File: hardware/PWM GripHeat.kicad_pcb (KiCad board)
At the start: 2 copper layers, 65 parts, among them J1 1770885, J2 1770898, J4 1770924, J5 0878340619, Q1 SiS415DNT, U1 ATtiny85-20P, U2 SiA462DJ, U3 LM324, U4 SiA462DJ

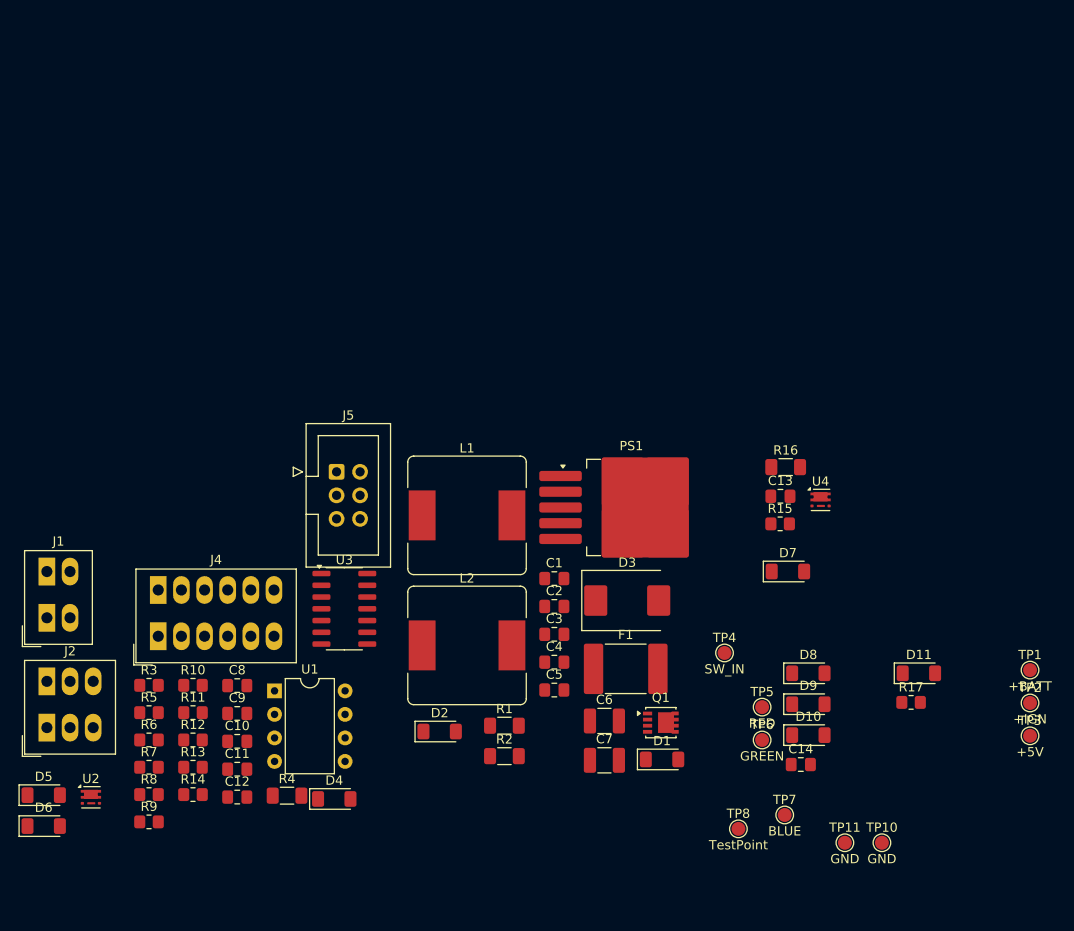
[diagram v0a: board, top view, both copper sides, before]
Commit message: PCB Basic outline
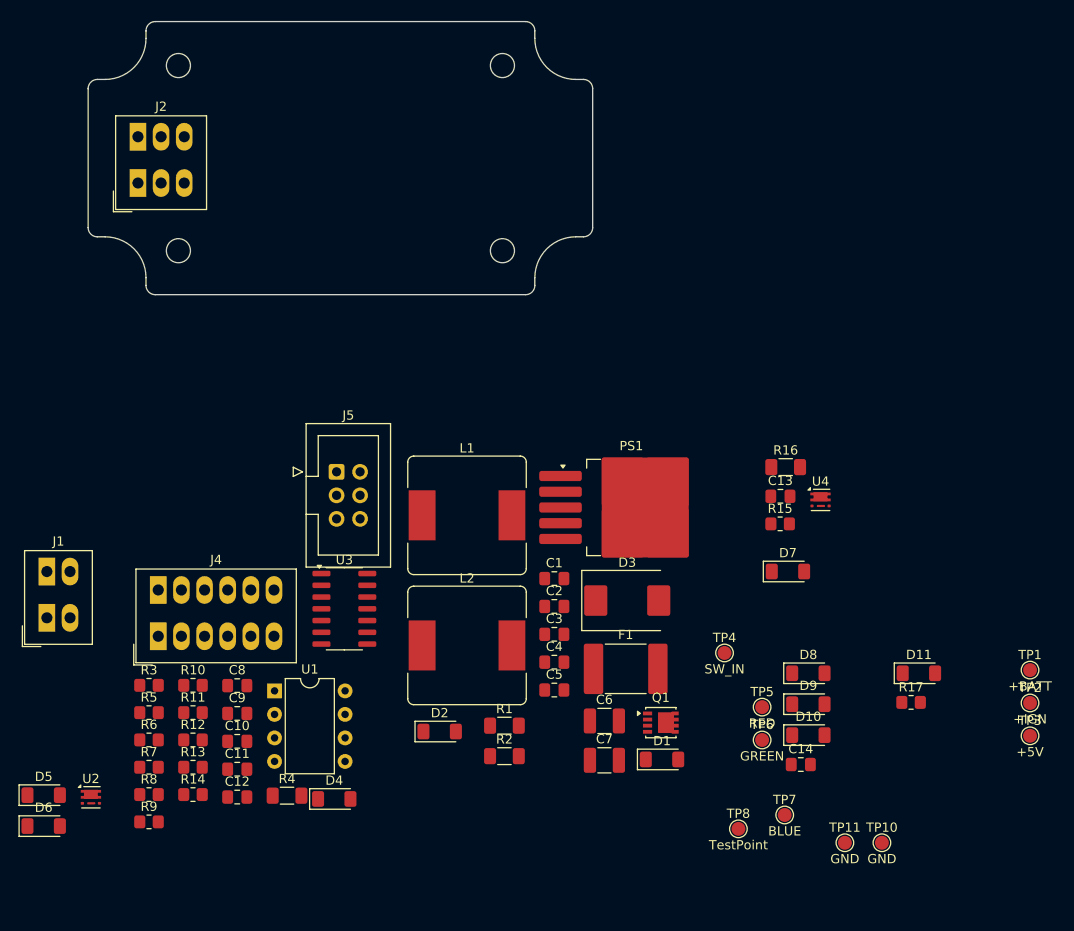
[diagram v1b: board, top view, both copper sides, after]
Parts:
- moved J2 59.6 mm to (142.1, 48.2)
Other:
- board outline added: 54.5 x 29.5 mm

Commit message: Pre DRC, almost done!
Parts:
- removed C6: EMK325ABJ107MM-T, Capacitor_SMD:C_1210_3225Metric_Pad1.33x2.70mm_HandSolder
- removed D3: B360, Diode_SMD:D_SMC
- removed D5: BZV55B18, Diode_SMD:D_MiniMELF
- removed J4: 1770924, TerminalBlock_Phoenix:TerminalBlock_Phoenix_PTSM-0,5-6-2.5-H-THR_1x06_P2.50mm_Horizontal
- removed J5: 0878340619, Connector_IDC:IDC-Header_2x03_P2.54mm_Vertical
- removed L2: 100uH, Inductor_SMD:L_Bourns_SRR1260
- removed Q1: SiS415DNT, Package_SO:Vishay_PowerPAK_1212-8_Single
- removed R1: 2.2k, Resistor_SMD:R_1206_3216Metric_Pad1.30x1.75mm_HandSolder
- removed R16: 100k, Resistor_SMD:R_1206_3216Metric_Pad1.30x1.75mm_HandSolder
- removed TP11: GND, TestPoint:TestPoint_Pad_D1.5mm
- removed U4: SiA462DJ, Package_TO_SOT_SMD:Vishay_PowerPAK_SC70-6L_Single
- added TP9: GND, TestPoint:TestPoint_THTPad_D2.0mm_Drill1.0mm, F.Cu at (138.6, 39.0)
- J1: footprint TerminalBlock_Phoenix:TerminalBlock_Phoenix_PTSM-0,5-2-2.5-H-THR_1x02_P2.50mm_Horizontal -> TerminalBlock:TerminalBlock_MaiXu_MX126-5.0-02P_1x02_P5.00mm
- J2: value 1770898 -> Screw_Terminal_01x08; footprint TerminalBlock_Phoenix:TerminalBlock_Phoenix_PTSM-0,5-3-2.5-H-THR_1x03_P2.50mm_Horizontal -> Connector_PinHeader_2.54mm:PinHeader_2x04_P2.54mm_Vertical
- L1: value 100uH -> 330uH; footprint Inductor_SMD:L_Bourns_SRR1260 -> myESP32s:L_Bourns_SRR7045
- PS1: value LM2576HVS-5 -> LMZM23600V5; footprint Package_TO_SOT_SMD:TO-263-5_TabPin3 -> Package_LGA:Texas_SIL0010A_MicroSiP-10-1EP_3.8x3mm_P0.6mm_EP0.7x2.9mm_ThermalVias
- TP10: footprint TestPoint:TestPoint_Pad_D1.5mm -> TestPoint:TestPoint_THTPad_D2.0mm_Drill1.0mm
- TP2: footprint TestPoint:TestPoint_Pad_D1.5mm -> TestPoint:TestPoint_THTPad_D1.0mm_Drill0.5mm
- TP6: value GREEN -> GRN
- TP8: value TestPoint -> PWM
- moved TP3 116.1 mm to (141.5, 44.2)
- moved TP10 95.3 mm to (183.2, 32.6)
- moved D11 94.3 mm to (145.3, 53.1), turned to 180 degrees
- moved TP1 92.5 mm to (160.7, 50.7)
- moved C14 92.5 mm to (155.9, 38.8), turned to 90 degrees
- moved R17 91.7 mm to (148.2, 55.3), turned to 180 degrees
- moved TP6 91.1 mm to (142.4, 46.8)
- moved TP2 88.3 mm to (171.8, 46.5)
- moved TP5 87.1 mm to (142.4, 49.4)
- moved TP7 86.8 mm to (160.0, 47.0)
- moved D6 85.4 mm to (171.4, 41.9), turned to 180 degrees
- moved D10 85.3 mm to (172.2, 33.8), turned to 90 degrees
- moved U2 84.4 mm to (187.5, 46.9), turned to 90 degrees
- moved D4 82.1 mm to (177.0, 33.8), turned to 90 degrees
- moved R14 82.0 mm to (161.1, 33.3)
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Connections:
- D1 pad 2: Net-(D1-A) -> GND
- J2 pad 1: /Power/+IGN -> +BATT
- J2 pad 2: +BATT -> +IGN
- PS1 pad 1: Net-(PS1-VIN) -> GND
- PS1 pad 2: Net-(D3-K) -> GND
- PS1 pad 3: GND -> Net-(PS1-VIN)
- PS1 pad 4: Net-(PS1-FB) -> Net-(D2-K)
- PS1 pad 5: Net-(PS1-~{ON}/OFF) -> unconnected-(PS1-PG-Pad5)
- R15 pad 1: /Power/+IGN -> +IGN
- R2 pad 1: Net-(PS1-~{ON}/OFF) -> Net-(D2-K)
- R2 pad 2: Net-(PS1-VIN) -> GND
- R5 pad 2: Net-(J4-Pin_5) -> Net-(J2-Pin_8)
- R6 pad 2: Net-(J4-Pin_4) -> Net-(J2-Pin_7)
- R7 pad 2: Net-(J4-Pin_3) -> Net-(J2-Pin_6)
- R8 pad 2: Net-(J4-Pin_2) -> Net-(J2-Pin_5)
- R9 pad 2: Net-(D5-K) -> Net-(J2-Pin_4)
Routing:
- net /PWM_out: track 0.00 -> 57.5 mm
- net +5V: track 0.00 -> 52.7 mm, vias 0 -> 2
- net +2V5: track 0.00 -> 45.6 mm, vias 0 -> 2
- net /GRN: track 0.00 -> 44.3 mm
- net Net-(D10-K): track 0.00 -> 31.0 mm
- net Net-(D2-K): track 0.00 -> 29.2 mm, vias 0 -> 1
- net /BLU: track 0.00 -> 27.5 mm, vias 0 -> 2
- net /RED: track 0.00 -> 26.0 mm
- net /SDO: track 0.00 -> 25.5 mm
- net +BATT: track 0.00 -> 25.1 mm
- net Net-(D6-K): track 0.00 -> 23.4 mm, vias 0 -> 3
- net Net-(D9-K): track 0.00 -> 23.2 mm
- net Net-(PS1-VIN): track 0.00 -> 18.3 mm
- net Net-(D4-K): track 0.00 -> 16.8 mm
- net Net-(D1-K): track 0.00 -> 12.8 mm
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- added copper zone on B.Cu, net GND
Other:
- outline, holes or cut-outs redrawn

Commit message: V1.0 release
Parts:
- added G***: LOGO, Atomspring Logos:10x10mm, B.Cu at (151.2, 101.1)
- moved C11 64.7 mm to (145.9, 104.9)
- moved D10 64.7 mm to (169.8, 98.5)
- moved L1 64.7 mm to (160.7, 120.3)
- moved PS1 64.7 mm to (152.1, 120.5)
- moved TP5 64.7 mm to (140.1, 114.0)
- moved C1 64.7 mm to (165.7, 122.5)
- moved C10 64.7 mm to (155.8, 104.8)
- moved C12 64.7 mm to (149.6, 101.7)
- moved C14 64.7 mm to (153.6, 103.5)
- moved C3 64.7 mm to (155.8, 118.5)
- moved C4 64.7 mm to (155.8, 122.3)
- moved C7 64.7 mm to (145.1, 122.8)
- moved C9 64.7 mm to (142.1, 104.9)
- moved D1 64.7 mm to (170.4, 117.5)
- moved D11 64.7 mm to (143.0, 117.8)
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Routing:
- net +2V5: track 45.6 -> 39.7 mm
- net GND: track 3.61 -> 7.97 mm, vias 1 -> 27
- net /PWM_out: track 57.5 -> 55.2 mm
- net /GRN: track 44.3 -> 45.1 mm
- net Net-(D6-K): vias 3 -> 2
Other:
- board text added: "+GRIPS"
- board text added: "-GRIPS"
- board text added: "BLU RED TO_SW +IGN"
- board text added: "GRN SW_IN GND +BATT"
- board text added: "PWM GripHeat - V1.0 atomspring"

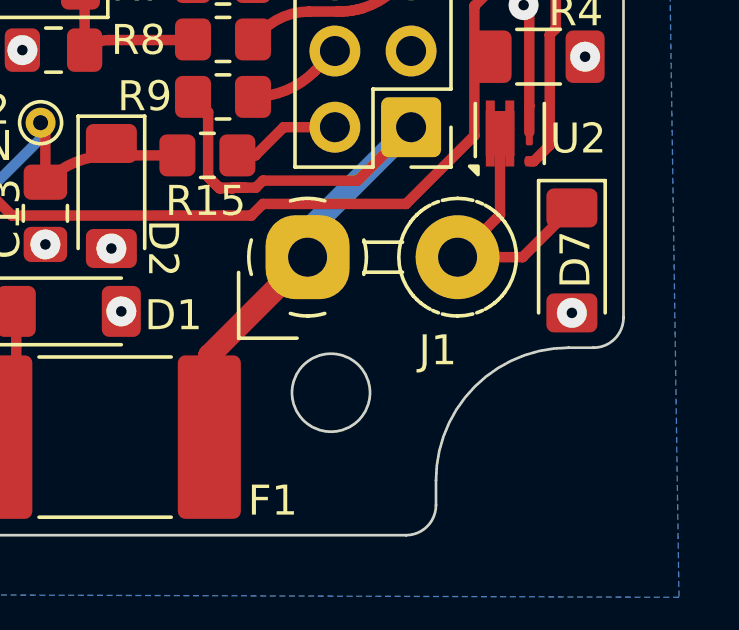
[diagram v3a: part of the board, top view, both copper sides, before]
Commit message: Improving documentation
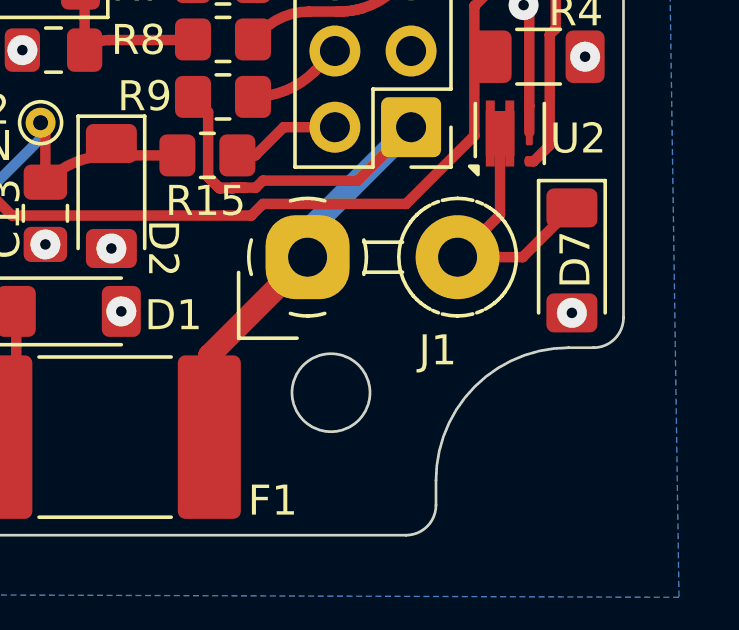
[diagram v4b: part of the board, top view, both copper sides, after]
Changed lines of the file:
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@@
 	(paper "USLetter")
 	(title_block
-		(title "PWM GripHeaet")
+		(title "PWM GripHeat")
 		(date "2024-12-02")
 		(rev "1.0")
@@
 		(fp_arc
 			(start 3.521125 1.286294)
-			(mid 3.477135 1.233898)
+			(mid 3.477135 1.233899)
 			(end 3.435 1.18)
 			(stroke
@@
 		(fp_arc
 			(start 3.904516 1.625664)
-			(mid 3.834647 1.576334)
+			(mid 3.834648 1.576333)
 			(end 3.767 1.524)
 			(stroke
@@
 		(fp_arc
 			(start 3.93363 -1.644317)
-			(mid 4.006369 -1.689268)
+			(mid 4.00637 -1.689265)
 			(end 4.081 -1.731)
 			(stroke
@@
 		(fp_arc
 			(start 4.080344 1.730739)
-			(mid 4.005725 1.688978)
+			(mid 4.005726 1.688977)
 			(end 3.933 1.644001)
 			(stroke
@@
 		(fp_arc
 			(start 5.000479 1.960685)
-			(mid 4.744554 1.943974)
+			(mid 4.744554 1.943973)
 			(end 4.493 1.894)
 			(stroke
@@
 		(fp_arc
 			(start 5.638712 -1.85392)
-			(mid 5.734863 -1.817952)
+			(mid 5.734863 -1.817951)
 			(end 5.829 -1.777)
 			(stroke
@@
 		(fp_arc
 			(start 5.829295 1.77705)
-			(mid 5.735154 1.818015)
+			(mid 5.735155 1.818016)
 			(end 5.639 1.854)
 			(stroke
@@
 		(fp_arc
 			(start 5.920652 -1.730826)
-			(mid 5.995272 -1.689019)
+			(mid 5.995273 -1.689021)
 			(end 6.067999 -1.644)
 			(stroke
@@
 		(fp_arc
 			(start 6.096479 -1.625751)
-			(mid 6.166349 -1.576375)
+			(mid 6.166348 -1.576374)
 			(end 6.234 -1.524)
 			(stroke
@@
 		(fp_arc
 			(start 6.36213 1.410651)
-			(mid 6.299299 1.468721)
+			(mid 6.2993 1.468722)
 			(end 6.234 1.524)
 			(stroke

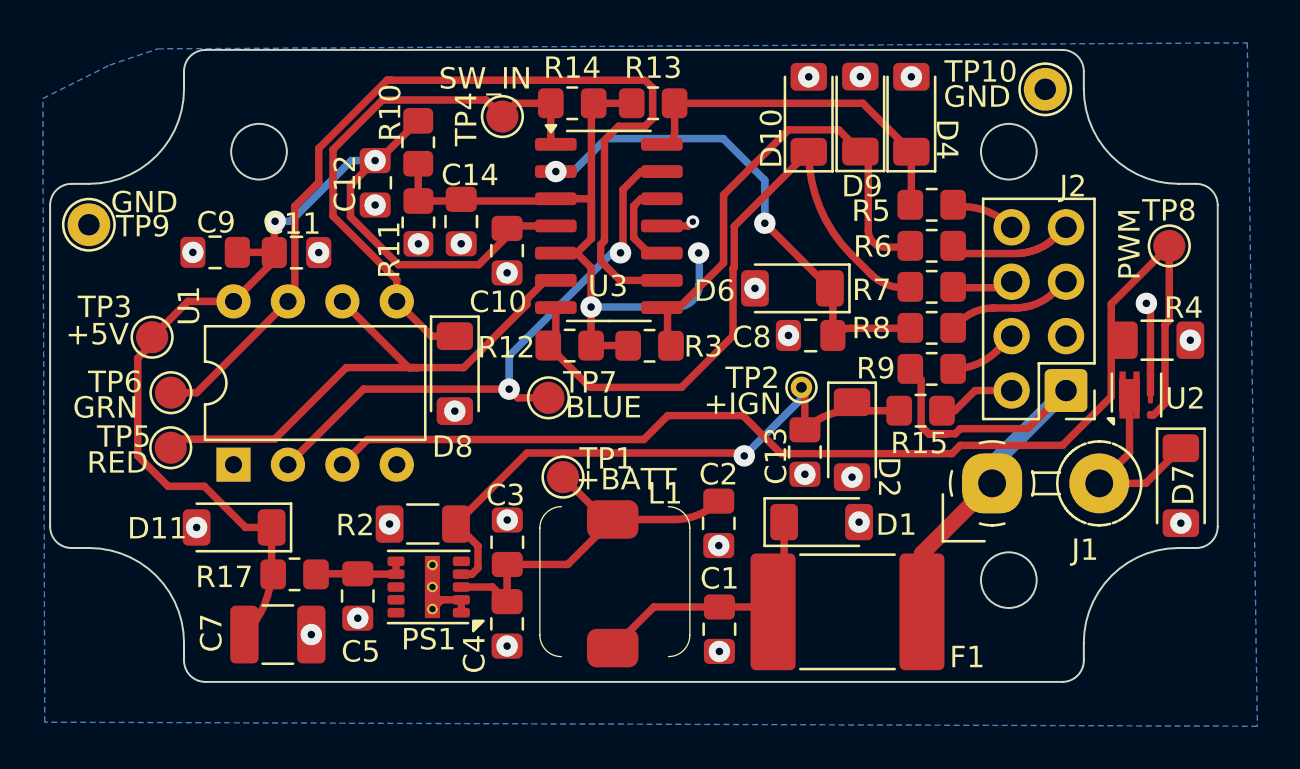
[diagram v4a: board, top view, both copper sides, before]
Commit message: Adding basic firmware, further docs
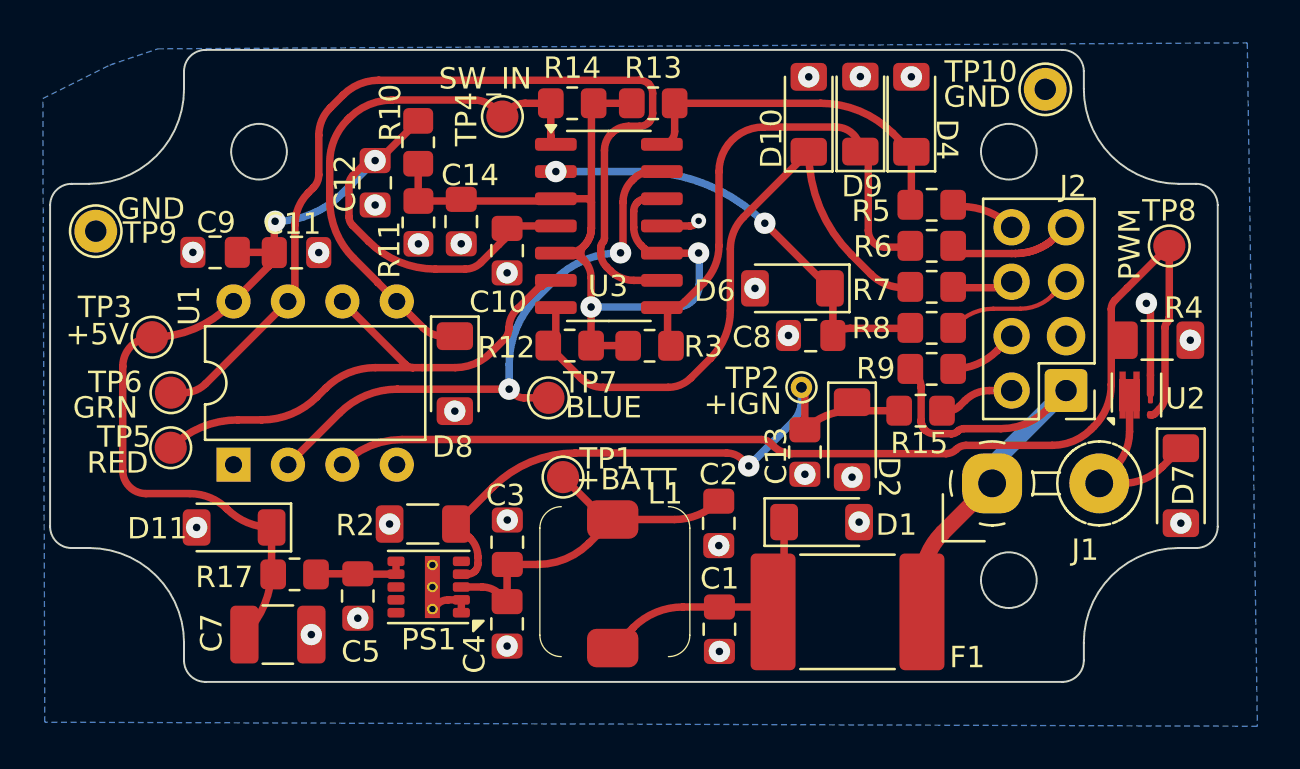
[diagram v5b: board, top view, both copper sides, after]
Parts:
- moved TP9 0.44 mm to (136.6, 103.9)
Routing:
- net +2V5: track 39.7 -> 42.6 mm
- net Net-(D6-K): track 23.4 -> 20.6 mm
- net +BATT: track 25.1 -> 23.7 mm
- net Net-(D7-K): track 9.20 -> 7.88 mm
- net /PWM_out: track 55.2 -> 53.9 mm
- net +5V: track 52.7 -> 53.8 mm
- net Net-(D9-K): track 23.1 -> 24.1 mm
- net /RED: track 26.0 -> 26.9 mm
- net Net-(J2-Pin_5): track 5.77 -> 6.36 mm
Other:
- board text added: "0"
- board text added: "0 mm"
- board text added: "0.01 mm"
- board text added: "0.02"
- board text added: "0.035 mm"
- board text added: "0.1500 mm"
- board text added: "0.2000 mm / 0.1500 mm"
- board text added: "1"
- board text added: "1.51 mm"
- board text added: "1.6000 mm"
- board text added: "2"
- board text added: "3.3"
- board text added: "4.5"
- board text added: "54.5000 mm x 29.5000 mm"
- board text added: "B.Cu"
- board text added: "B.Mask"
- board text added: "B.Paste"
- board text added: "B.Silkscreen"
- board text added: "BOARD CHARACTERISTICS"
- board text added: "Board Thickness:"
- board text added: "Board overall dimensions:"
- board text added: "Bottom Silk Screen"
- board text added: "Bottom Solder Mask"
- board text added: "Bottom Solder Paste"
- board text added: "Castellated pads:"
- board text added: "Color"
- board text added: "Copper Finish:"
- board text added: "Copper Layer Count:"
- board text added: "Dielectric 1"
- board text added: "ENIG"
- board text added: "Edge card connectors:"
- board text added: "Epsilon R"
- board text added: "F.Cu"
- board text added: "F.Mask"
- board text added: "F.Paste"
- board text added: "F.Silkscreen"
- board text added: "FR4"
- board text added: "Impedance Control:"
- board text added: "Layer Name"
- board text added: "Loss Tangent"
- board text added: "Material"
- board text added: "Min hole diameter:"
- board text added: "Min track/spacing:"
- board text added: "No"
- board text added: "Not specified"
- board text added: "Plated Board Edge:"
- board text added: "Thickness (mm)"
- board text added: "Top Silk Screen"
- board text added: "Top Solder Mask"
- board text added: "Top Solder Paste"
- board text added: "Type"
- board text added: "copper"
- board text added: "core"

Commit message: Released
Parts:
- moved G*** 0.30 mm to (151.0, 101.3)
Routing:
- net /BLU: track 27.8 -> 28.4 mm
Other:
- rule pad_to_mask_clearance: 0 -> 0.0508
- board text added: "Epoxy"
- board text added: "FR4 natural"
- board text added: "Purple"
- board text added: "White"
